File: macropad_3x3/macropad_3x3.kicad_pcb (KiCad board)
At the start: 2 copper layers, 57.1 x 57.1 mm, 36 parts, among them Q1 2N7002, U1 TRRS

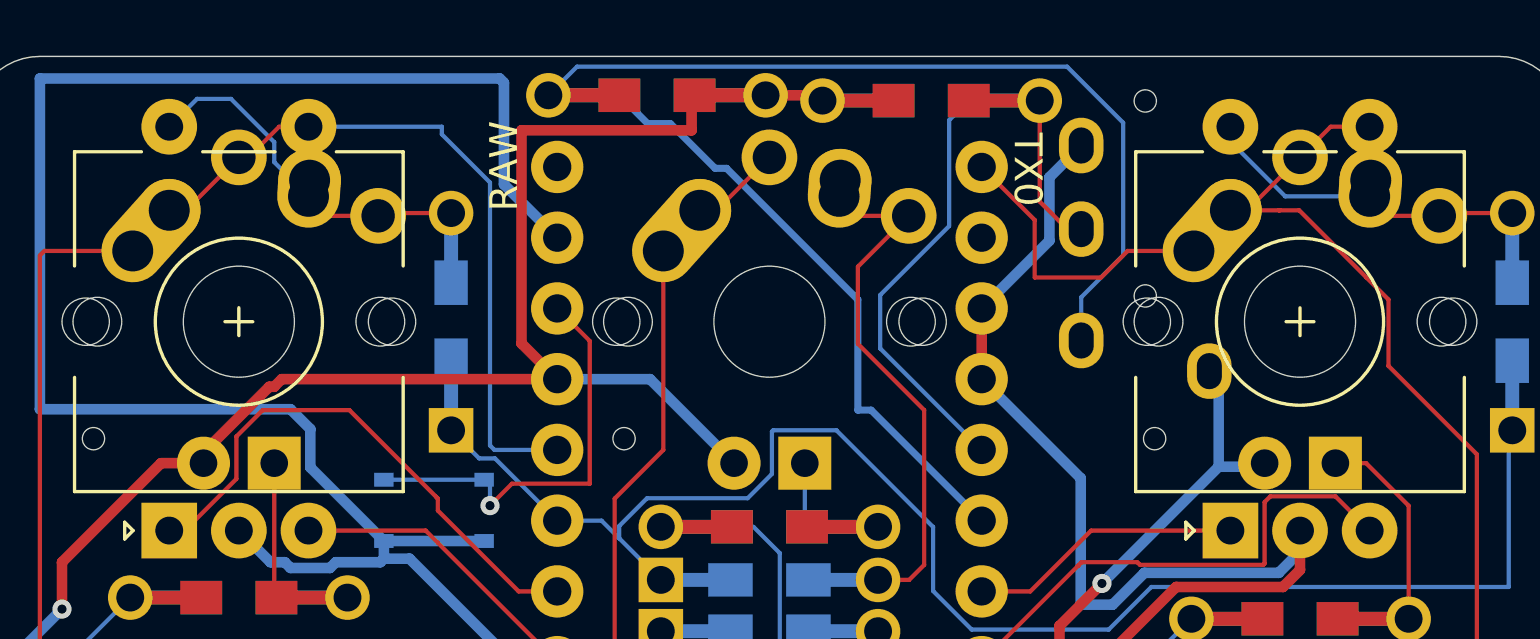
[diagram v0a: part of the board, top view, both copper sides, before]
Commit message: 3x3 macropad v2
Updated the 3x3 macropad project to fix the issue with the rotary encoders causing the top corners to always be bridged. Slightly moved the TRRS jack further from the top right switch to give a bit more clearance for the rotary encoder pins.
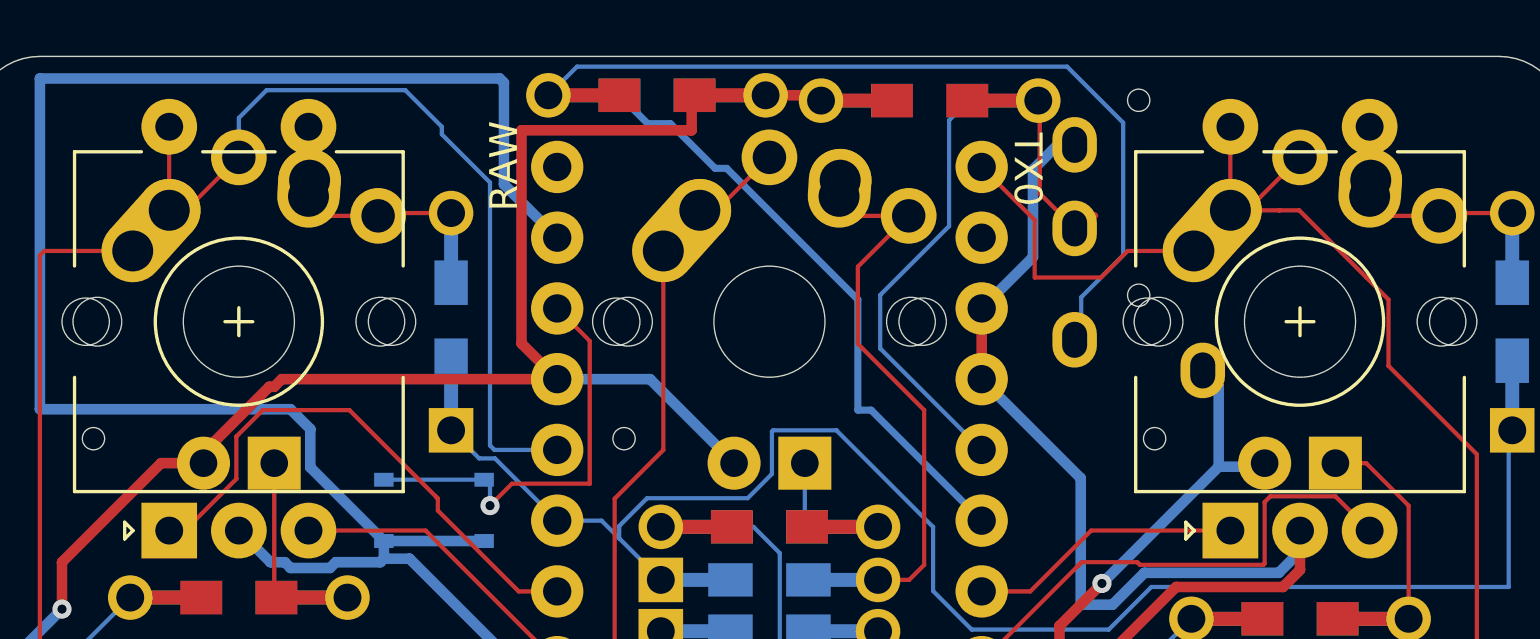
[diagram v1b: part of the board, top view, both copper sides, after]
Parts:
- B1: value PRO_MICRO -> SPARKFUN_PRO_MICRO
- moved U1 0.24 mm to (64.1, 22.2)
- moved R11 0.05 mm to (56.6, 23.8)
- renumbered reset to reset1
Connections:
- RE1 pad S1: col0 -> Net-(D1-Pad2)
- RE1 pad S2: Net-(D1-Pad2) -> col0
- RE2 pad S1: col2 -> Net-(D3-Pad2)
- RE2 pad S2: Net-(D3-Pad2) -> col2
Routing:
- net Net-(D1-Pad2): track 12.7 -> 7.39 mm
- net col0: track 79.9 -> 85.2 mm
- net Net-(D3-Pad2): track 11.8 -> 7.39 mm
- net VCC: track 246.2 -> 246.8 mm
- net col2: track 87.0 -> 87.5 mm
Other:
- board text added: "3x3 macropad v2"
- board text removed: "3x3 macropad v2b1"
